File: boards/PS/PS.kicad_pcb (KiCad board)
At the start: 2 copper layers, 120 x 100 mm, 24 parts, among them K1 NRP-15-C-24D, U1 Модуль XL4015E, U2 VRB2405YMD-10WR3, X1 DG301-5.0-02P-12, X10 DG301-5.0-02P-12, X11 B2B-XH-A, X2 B4B-XH-A, X3 B2P-VH, X4 B2P-VH, X5 B2B-XH-A, X6 DG301-5.0-02P-12, X7 DG301-5.0-02P-12, X8 DG301-5.0-02P-12, X9 DG301-5.0-02P-12

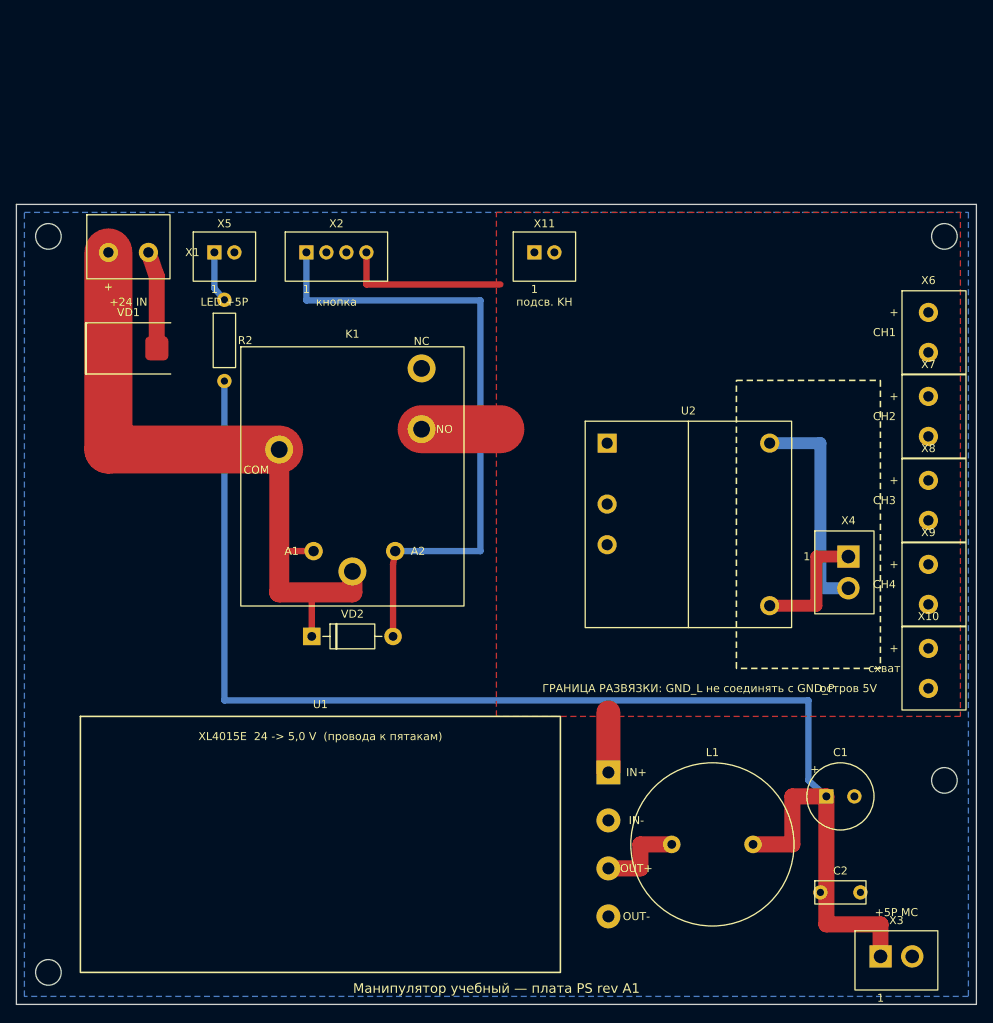
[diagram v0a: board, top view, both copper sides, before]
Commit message: Платы PS, MC, CH, LR: расстановка, трассировка, 3D-модели посадочных мест
PS:
- разведена по расстановке из файла: +24V_IN 6 мм (участок у K1 — 4 мм),
  шина +24V 6 мм с отводами 3 мм, +5P 2 мм, остров U2 1,5 мм;
  заливка GND_P на B.Cu, вырез заливки под островом, вырезы ⌀8 у крепежа
- классы цепей в PS.kicad_pro: Default, Power5, Power24, Island
- U1: посадочное место под модуль XL4015E 54 × 24 × 15 на штырях
  (пятаки IN/OUT, 2 стойки М3) по чертежу продавца; переразведены
  OUT+ и отвод +24V к IN+

MC:
- X5 перенесён, переразведены KH, +5P, GND_P в этой зоне
- FU1: место под Bourns MF-R110 (корпус 8,9 × 3,0 × 14,0)

CH:
- K1…K5, X5: места исправлены по datasheet (NRP-02, HF49FD, JST VH),
  переразведены цепи реле

LR:
- плата перекомпонована: X5…X8 — B5B-XH-A, как X1…X4; группы M1…M4
  по одному образцу (индикатор, разъём, защита в два ряда);
  X1…X4, X9 и DD1 на нижней стороне
- контур 176 × 59, 6 отверстий М3; разведена: сигналы F.Cu,
  GND_L заливкой B.Cu
- scripts/gen_LR_pcb.py удалён: описывал прежнюю раскладку с клеммами

Схемы:
- CH: X5 — JST VH (таблица Tbl_X5_CH_VH); MC: X3 — B4B-XH-A
  (кнопка KH с индикатором); PS: X11 убран; LR: у X5…X8 место
  B5B-XH-A
- sch_common: генератор не перезаписывает файл, сохранённый KiCad,
  без --force

3D-модели (lib/3dmodels):
- упрощённые по чертежам datasheet: NRP-02, HF49FD, NRP-15 (корпус),
  JST B2P-VH, Mornsun/K-CUT URB2405YMD (U2), Talema DPO-3.0-22 (кольцо
  лежит), Bourns MF-R110
- из библиотеки KiCad: PinSocket 1×3, 1×4, 1×12, Phoenix MKDS-1,5-2
- docs/3D-модели.md — источники размеров и что сверить

База компонентов: E-083 — Bourns MF-R110 (Ihold 1,1 А), «Выбран»;
csv перевыгружены
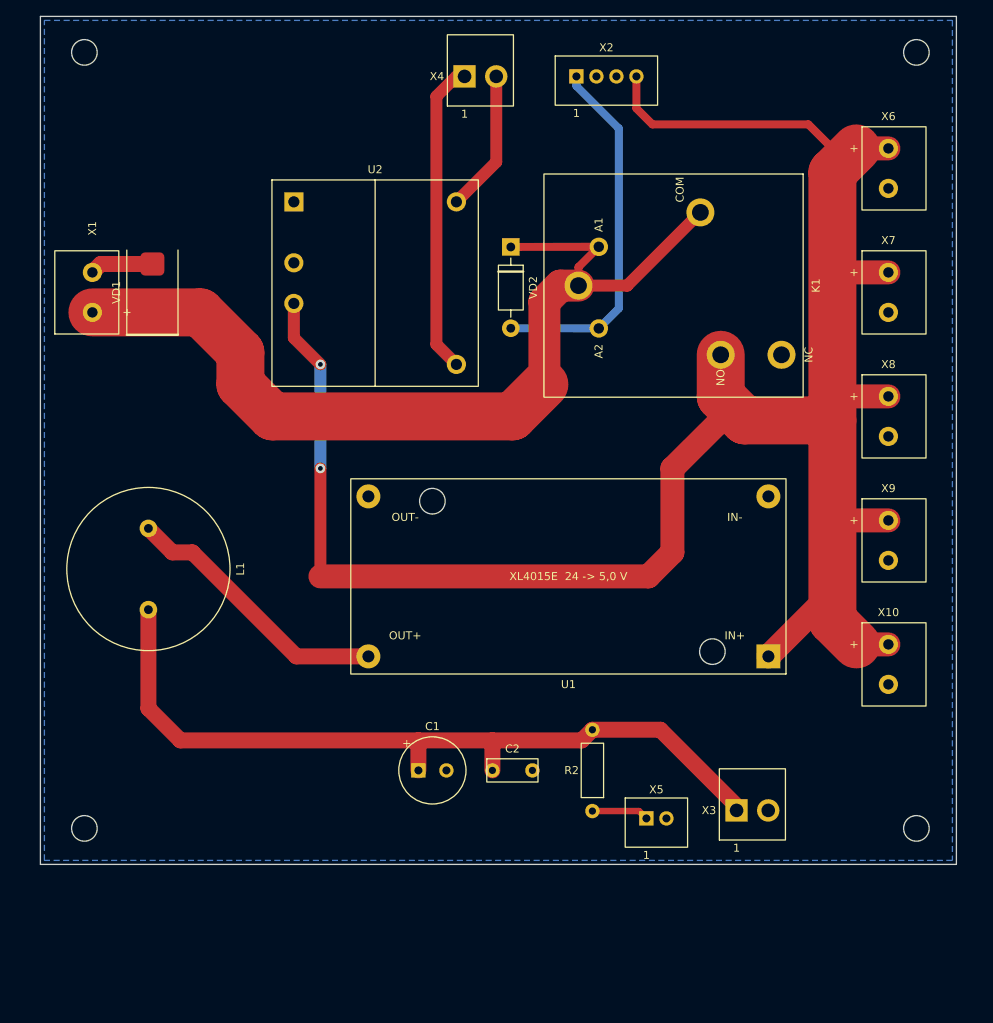
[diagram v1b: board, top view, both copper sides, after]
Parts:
- removed X11: B2B-XH-A, manipulator:JST_XH_B2B-XH-A
- X3: footprint manipulator:JST_VH_B2P-VH -> manipulator:JST_VH_B2P-VH_V
- moved X5 89.0 mm to (130.0, 126.8)
- moved L1 78.5 mm to (66.5, 95.6), turned to -90 degrees
- moved X4 77.2 mm to (108.0, 34.0), turned to 90 degrees
- moved R2 70.7 mm to (122.0, 120.8), turned to 180 degrees
- moved C1 51.1 mm to (102.0, 120.8)
- moved U2 49.4 mm to (94.8, 59.8)
- moved VD2 47.9 mm to (111.8, 60.4), turned to -90 degrees
- moved K1 46.7 mm to (132.1, 60.1), turned to -90 degrees
- moved U1 45.6 mm to (119.0, 96.5), turned to 180 degrees
- moved C2 43.7 mm to (112.0, 120.8)
- moved X2 40.3 mm to (123.8, 34.0)
- moved X3 25.6 mm to (142.0, 125.8), turned to 90 degrees
- moved H1 23.4 mm to (58.5, 31.0)
- moved H2 23.3 mm to (162.5, 31.0)
- moved X6 21.1 mm to (159.0, 45.5)
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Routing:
- net +24V: track 38.1 -> 257.6 mm, vias 0 -> 2
- net +5P: track 167.9 -> 100.1 mm
- net Net-(K1-A2): track 80.4 -> 45.7 mm
- net +24V_IN: track 85.4 -> 117.3 mm
- net Net-(U1-OUT+): track 10.9 -> 34.1 mm
- net Net-(U2-+Vo): track 16.0 -> 39.1 mm
- net Net-(U2-0V): track 28.0 -> 17.7 mm
- net GND_P: track 12.2 -> 7.93 mm
- net Net-(X5-LED): track 6.39 -> 7.13 mm
- removed copper zone on F.Cu, net +24V
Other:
- board size 120 x 100 mm -> 114.5 x 106 mm
- rule pad_to_mask_clearance: 0.05 -> 0
- board text removed: "+24 IN"
- board text removed: "+5P MC"
- board text removed: "CH1"
- board text removed: "CH2"
- board text removed: "CH3"
- board text removed: "CH4"
- board text removed: "LED +5P"
- board text removed: "ГРАНИЦА РАЗВЯЗКИ: GND_L не соединять с GND_P"
- board text removed: "Манипулятор учебный — плата PS rev A1"
- board text removed: "кнопка"
- board text removed: "остров 5V"
- board text removed: "подсв. KH"
- board text removed: "схват"
